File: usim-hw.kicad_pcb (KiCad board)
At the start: 2 copper layers, 110.5 x 63.5 mm, 35 parts, among them J2 Conn_01x06, SW1 SW_SPST, U1 MC6809, U2 MC6850, U3 62256, U4 28C256, U5 NE555P, U6 74LS10, U7 74LS04, Y1 2.4576M

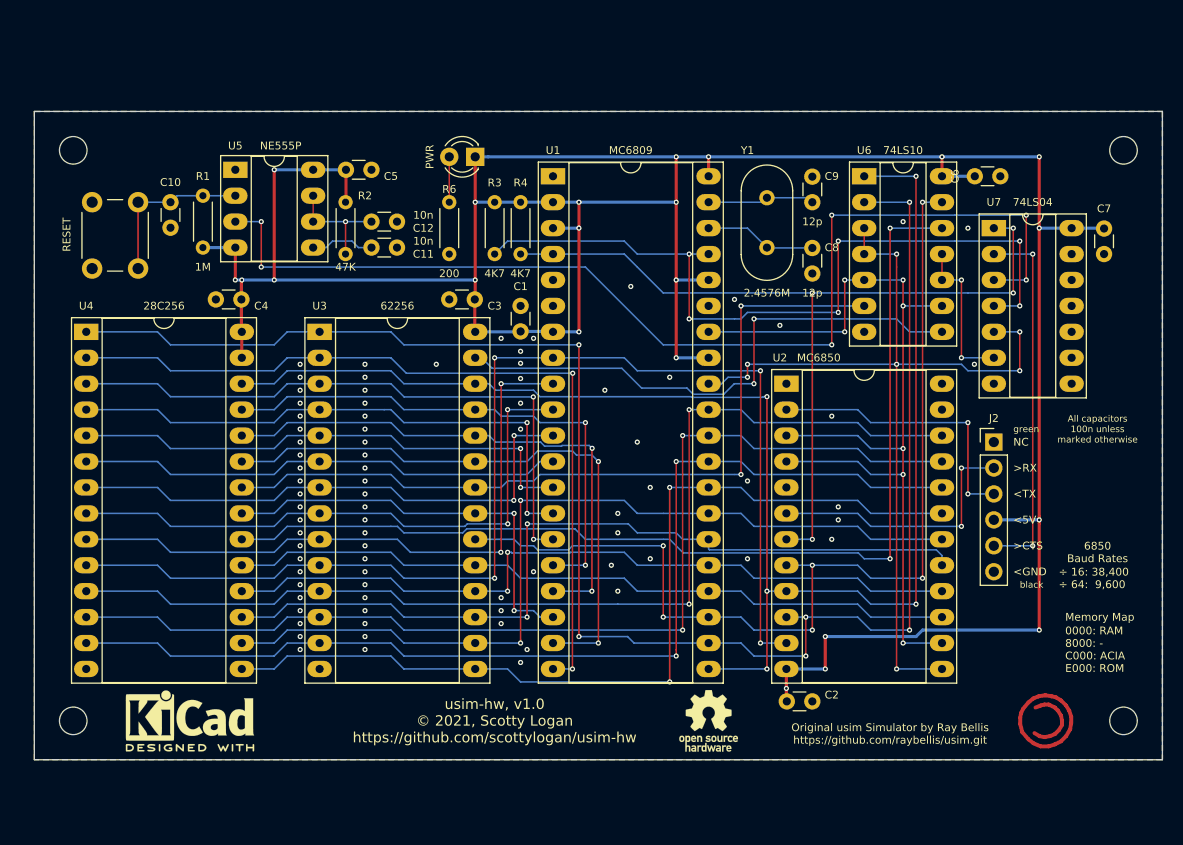
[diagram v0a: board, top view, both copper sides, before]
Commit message: saved zif-less pcb
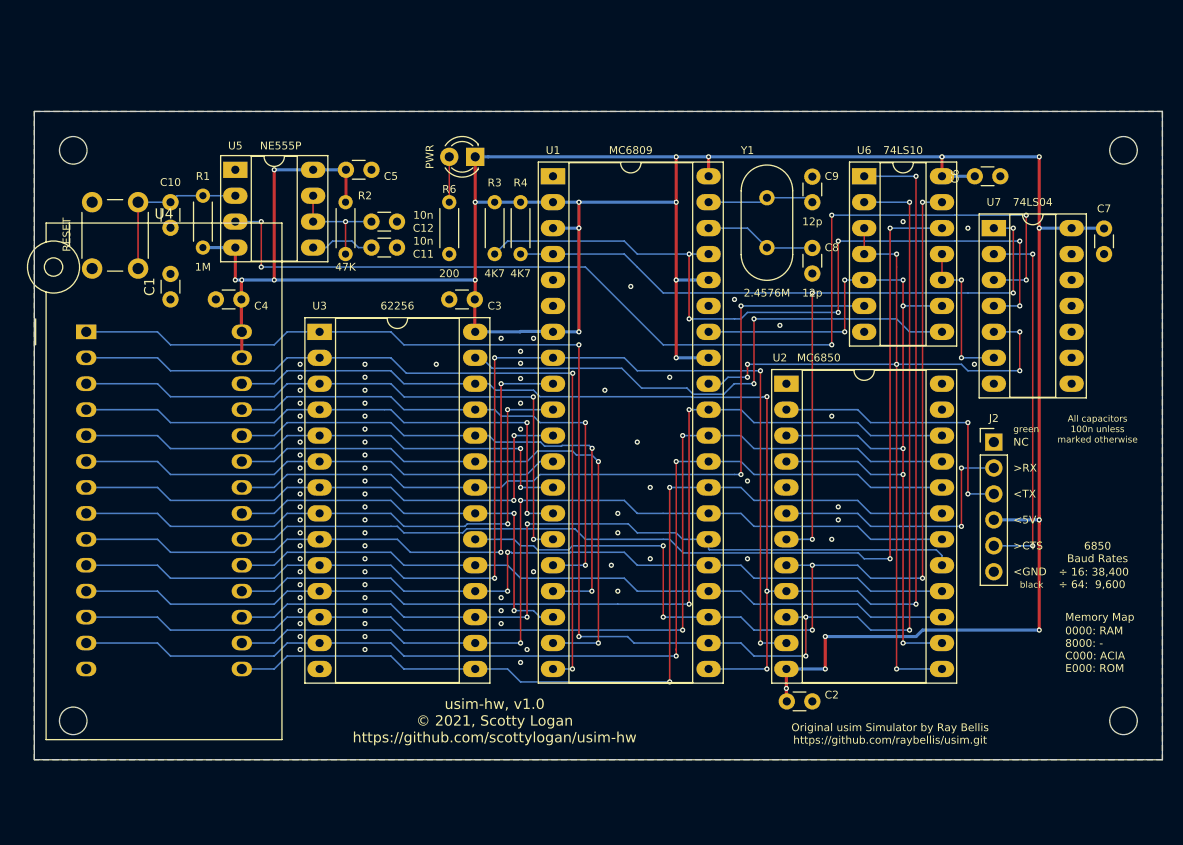
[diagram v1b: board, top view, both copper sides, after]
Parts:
- removed REF**: OSHW-Logo_5.7x6mm_SilkScreen, Symbol:OSHW-Logo_5.7x6mm_SilkScreen
- removed REF**: KiCad-Logo2_5mm_SilkScreen, Symbol:KiCad-Logo2_5mm_SilkScreen
- removed REF**: Symbol_CC-ShareAlike_CopperTop_Small, Symbol:Symbol_CC-ShareAlike_CopperTop_Small
- U4: footprint Package_DIP:DIP-28_W15.24mm_Socket_LongPads -> Socket:DIP_Socket-28_W11.9_W12.7_W15.24_W17.78_W18.5_3M_228-1277-00-0602J
- moved C1 34.3 mm to (64.1, 62.9), turned to 90 degrees

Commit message: switched to ZIF for EEPROM, shrunk by removing mt. holes
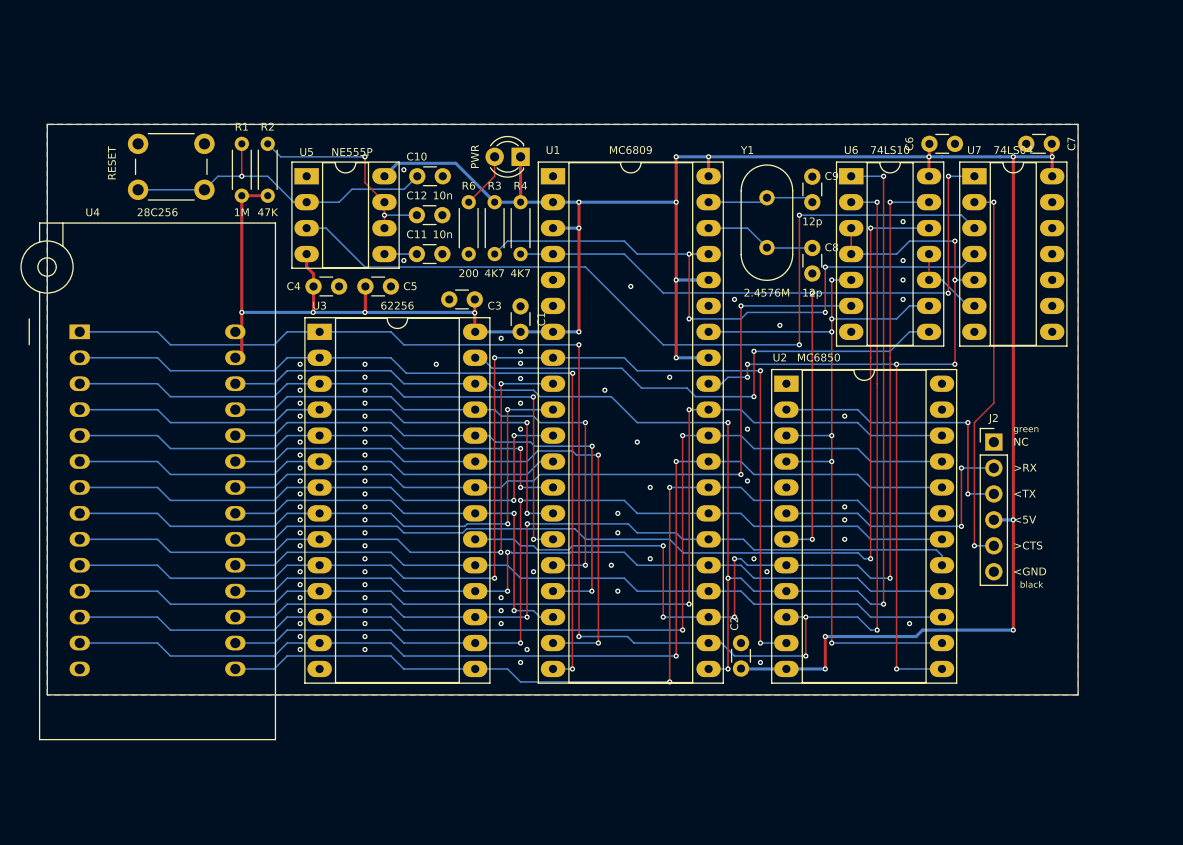
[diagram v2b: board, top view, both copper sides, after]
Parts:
- removed H1, H2, H3, H4: MountingHole, MountingHole:MountingHole_2.7mm_M2.5
- moved C1 34.3 mm to (98.4, 63.5), turned to 270 degrees
- moved C10 27.1 mm to (90.8, 50.8), turned to 180 degrees
- moved C7 13.2 mm to (148.0, 47.6), turned to 0 degrees
- moved SW1 13.0 mm to (61.0, 47.6), turned to 0 degrees
- moved C4 12.1 mm to (80.6, 61.6), turned to 180 degrees
- moved C5 11.6 mm to (85.7, 61.6)
- moved C2 9.03 mm to (120.0, 96.5), turned to 270 degrees
- moved R2 7.65 mm to (73.7, 52.7), turned to 90 degrees
- moved U5 7.01 mm to (77.5, 50.8)
- moved R1 6.35 mm to (71.1, 47.6)
- moved C6 5.46 mm to (141.0, 47.6)
- moved U7 5.43 mm to (142.9, 50.8)
- moved C11 4.49 mm to (88.3, 58.4)
- moved C12 4.49 mm to (88.3, 54.6)
- moved D3 4.44 mm to (98.4, 48.9)
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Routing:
- net VCC: track 297.6 -> 263.2 mm, vias 22 -> 19
- net /RESET: track 107.3 -> 83.4 mm, vias 6 -> 2
- net Net-(C10-Pad2): track 16.9 -> 33.2 mm
- net /~RESET: track 76.9 -> 61.5 mm, vias 6 -> 4
- net /E: track 91.2 -> 79.3 mm, vias 7 -> 6
- net /A13: track 147.6 -> 137.7 mm
- net Net-(C12-Pad1): track 11.4 -> 21.0 mm, vias 1 -> 2
- net /~R~W: track 15.2 -> 8.04 mm, vias 2 -> 0
- net /A14: track 164.2 -> 159.1 mm
- net /A15: track 100.1 -> 95.4 mm
- net /~WR: track 54.5 -> 51.3 mm
- net Net-(C11-Pad1): track 6.24 -> 3.17 mm
- net /R~W: track 89.4 -> 87.1 mm
- net /~CTS: track 36.2 -> 38.3 mm
- net /~RD: track 79.0 -> 77.8 mm
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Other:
- board size 110.5 x 63.5 mm -> 101 x 55.9 mm
- board text added: "0000-7FFF RAM C000-C001 ACIA E000-FFFF ROM"
- board text removed: "0000: RAM 8000: - C000: ACIA E000: ROM"

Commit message: removed memory to shrink design; use separate memory board
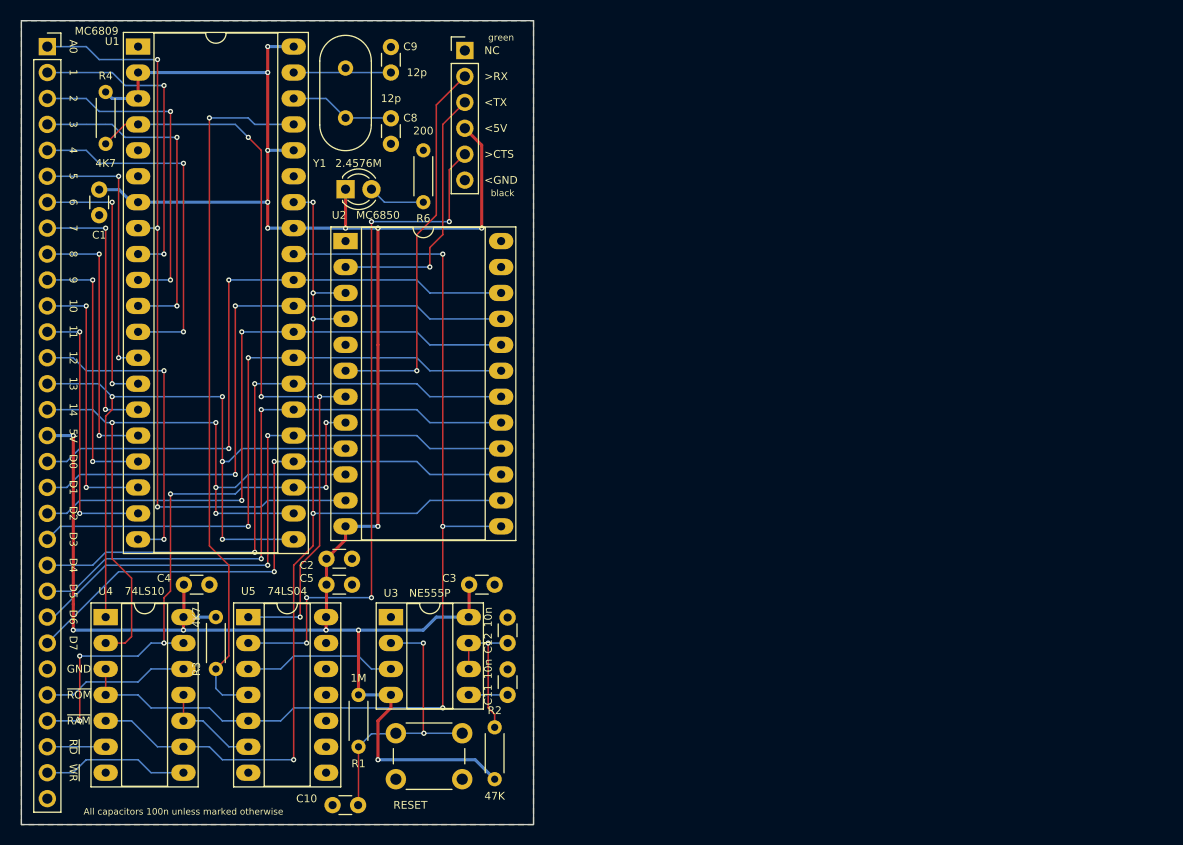
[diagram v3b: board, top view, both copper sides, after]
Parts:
- removed C6, C7: 100n, Capacitor_THT:C_Disc_D3.0mm_W1.6mm_P2.50mm
- removed the U3 at (78.7, 66.0)
- removed U6: 74LS10, Package_DIP:DIP-14_W7.62mm_Socket_LongPads
- added J1: Conn_01x30_Female, Connector_PinSocket_2.54mm:PinSocket_1x30_P2.54mm_Vertical, F.Cu at (52.1, 38.1)
- U4: value 28C256 -> 74LS10; footprint Socket:DIP_Socket-28_W11.9_W12.7_W15.24_W17.78_W18.5_3M_228-1277-00-0602J -> Package_DIP:DIP-14_W7.62mm_Socket_LongPads
- moved U5 83.2 mm to (71.8, 94.0)
- moved SW1 69.9 mm to (92.7, 109.9), turned to 180 degrees
- moved J2 64.5 mm to (93.0, 38.5)
- moved C10 62.5 mm to (80.0, 112.4), turned to 0 degrees
- moved R2 61.3 mm to (95.9, 109.9)
- moved R1 60.2 mm to (82.5, 106.7), turned to 90 degrees
- moved R3 49.0 mm to (68.6, 94.0)
- moved U2 45.4 mm to (81.3, 57.1)
- moved C11 44.1 mm to (97.2, 101.6), turned to 90 degrees
- moved U3 44.0 mm to (85.7, 94.0)
- moved C8 43.2 mm to (85.7, 47.6)
- moved C9 43.2 mm to (85.7, 40.6)
- moved Y1 43.2 mm to (81.3, 45.1)
- moved C12 42.8 mm to (97.2, 96.5), turned to 90 degrees
- moved U1 42.6 mm to (61.0, 38.1)
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- renumbered U5 to U3, U7 to U5
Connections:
- U4 pad 1: /A14 -> /A13
- U4 pad 10: /A0 -> /~R~W
- U4 pad 11: /D0 -> /~R~W
- U4 pad 12: /D1 -> /~ROM
- U4 pad 13: /D2 -> /A15
- U4 pad 14: GND -> VCC
- U4 pad 2: /A12 -> /A14
- U4 pad 3: /A7 -> /R~W
- U4 pad 4: /A6 -> /R~W
- U4 pad 5: /A5 -> /E
- U4 pad 6: /A4 -> /~RD
- U4 pad 7: /A3 -> GND
- U4 pad 8: /A2 -> /~WR
- U4 pad 9: /A1 -> /E
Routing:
- net /A14: track 159.1 -> 71.3 mm, vias 6 -> 4
- net /~ROM: track 101.9 -> 14.4 mm, vias 2 -> 0
- net /~RD: track 77.8 -> 5.71 mm, vias 2 -> 0
- net /RESET: track 83.4 -> 15.0 mm, vias 2 -> 0
- net /A13: track 137.7 -> 73.1 mm, vias 5 -> 4
- net /A12: track 80.2 -> 31.0 mm
- net /D2: track 105.5 -> 62.0 mm
- net /D0: track 105.5 -> 62.0 mm
- net /D1: track 105.5 -> 62.0 mm
- net /A0: track 118.9 -> 75.7 mm, vias 4 -> 3
- net /~WR: track 51.3 -> 14.4 mm, vias 2 -> 0
- net /A15: track 95.4 -> 58.8 mm
- net /A7: track 61.2 -> 26.7 mm
- net /A1: track 63.8 -> 31.0 mm
- net /A11: track 59.4 -> 26.7 mm
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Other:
- board size 101 x 55.9 mm -> 50.2 x 78.7 mm
- board text added: "1"
- board text added: "10"
- board text added: "11"
- board text added: "12"
- board text added: "13"
- board text added: "14"
- board text added: "2"
- board text added: "3"
- board text added: "4"
- board text added: "5"
- board text added: "5V"
- board text added: "6"
- board text added: "7"
- board text added: "8"
- board text added: "9"
- board text added: "A0"
- board text added: "D0"
- board text added: "D1"
- board text added: "D2"
- board text added: "D3"
- board text added: "D4"
- board text added: "D5"
- board text added: "D6"
- board text added: "D7"
- board text added: "GND"
- board text added: "~RAM"
- board text added: "~RD"
- board text added: "~ROM"
- board text added: "~WR"

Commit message: updated labels
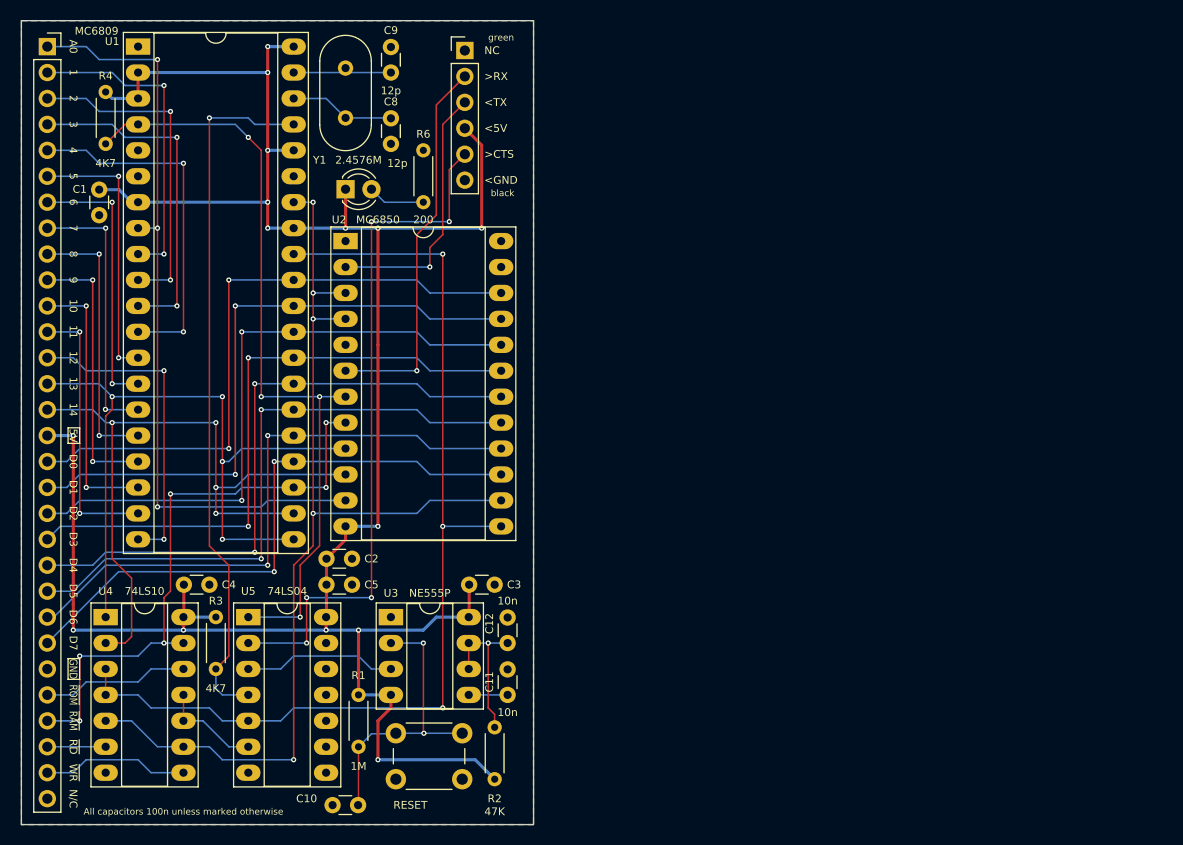
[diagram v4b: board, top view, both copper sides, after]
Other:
- board text added: "0000-7FFF C000-C001 E000-FFFF"
- board text added: "38,400 9,600"
- board text added: "N/C"
- board text added: "RAM ACIA ROM"
- board text added: "usim-hw, v1.1 © 2021, Scotty Logan https://github.com/scottylogan/usim-hw"
- board text added: "÷16 ÷64"
- board text removed: "0000-7FFF RAM C000-C001 ACIA E000-FFFF ROM"
- board text removed: "usim-hw, v1.0 © 2021, Scotty Logan https://github.com/scottylogan/usim-hw"
- board text removed: "÷ 16: 38,400 ÷ 64: 9,600"
